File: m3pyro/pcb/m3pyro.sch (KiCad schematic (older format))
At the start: 54 parts, among them IC1 STM32F405RxTx, IC2 MCP2562, J10 WEST BOT, J11 EAST TOP, J12 EAST BOT, J9 WEST TOP, Q1 2FET2, Q2 2FET2, Q3 2FET2, Q4 2FET2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

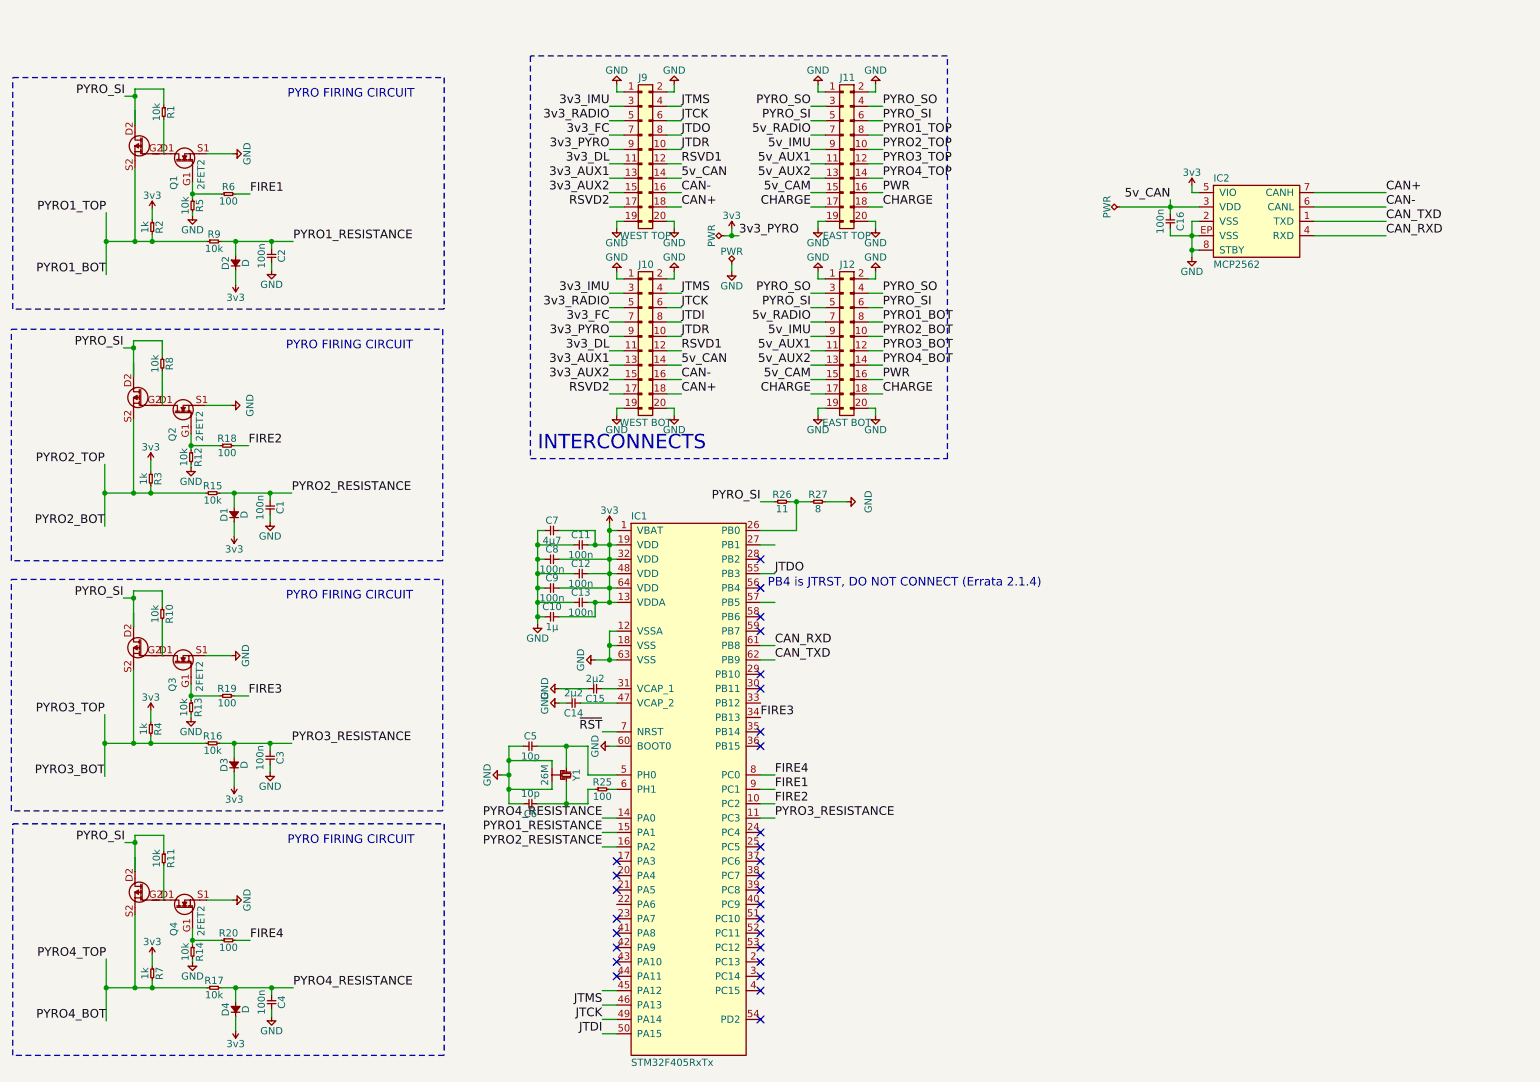
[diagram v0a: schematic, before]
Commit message: schematic in line?
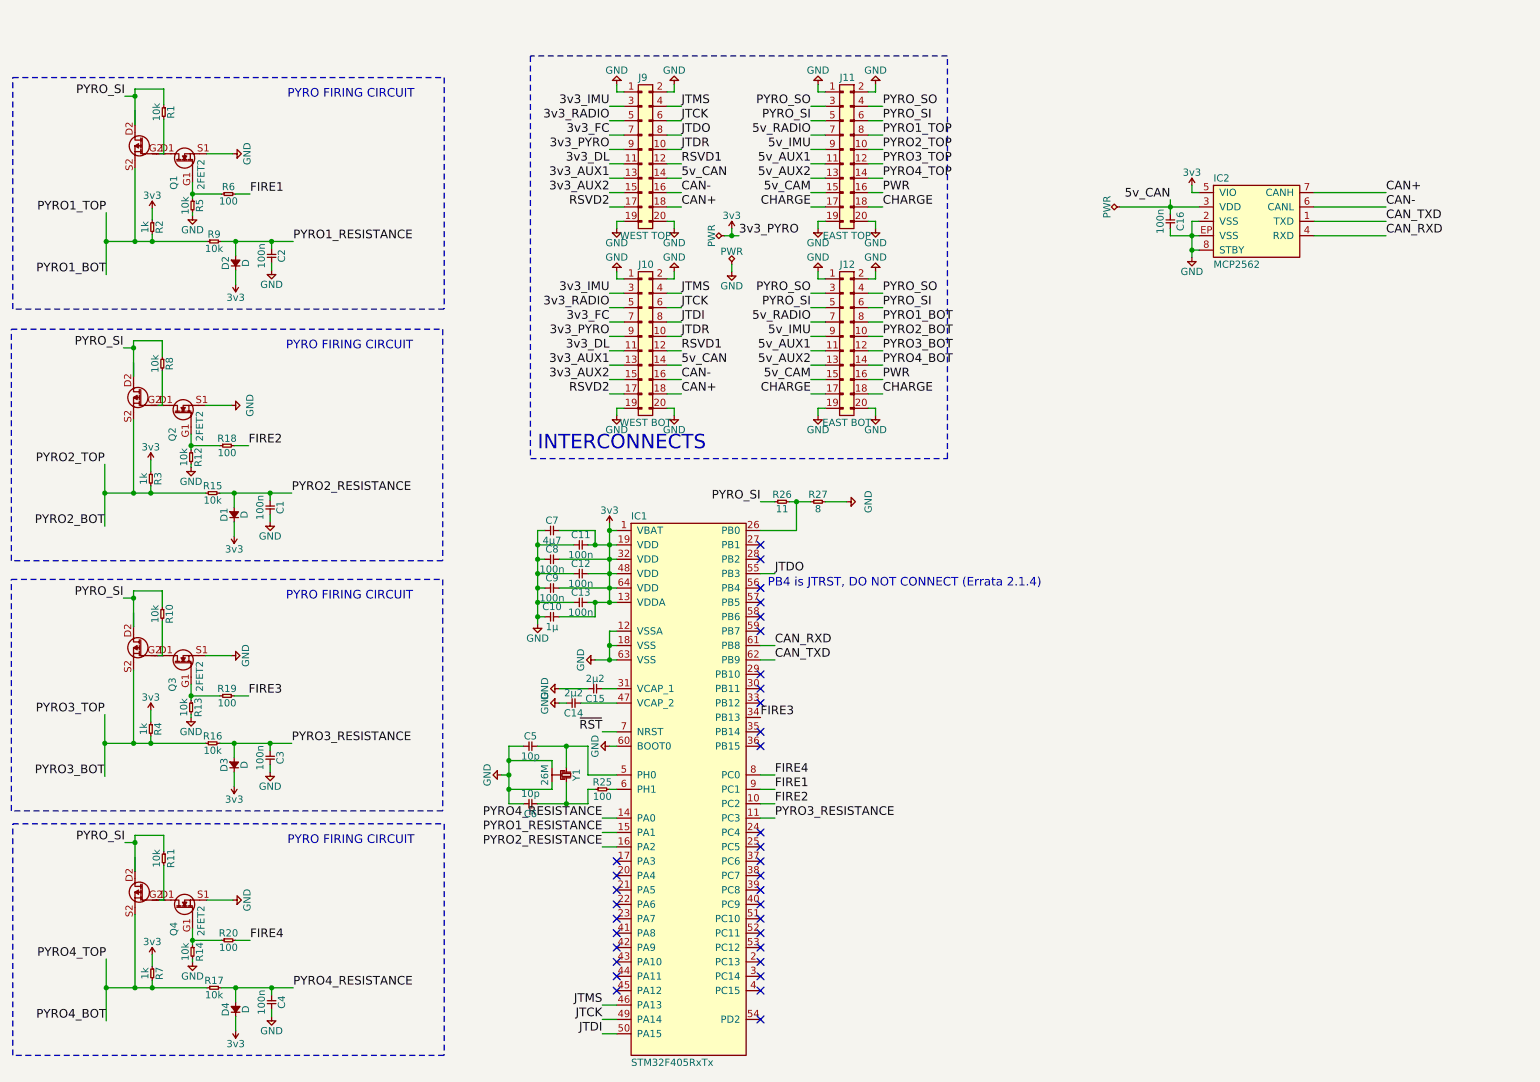
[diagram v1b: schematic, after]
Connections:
- net at Q1.D1, R1.2: now also Q1.G2
- net at Q2.D1, R8.2: now also Q2.G2
- net at Q3.D1, R10.2: now also Q3.G2
- net at Q4.D1, R11.2: now also Q4.G2
- no-connect marks 29 -> 34
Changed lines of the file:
@@
 	4750 7250 4650 7250
-Wire Wire Line
-	5750 4050 5850 4050
-Wire Wire Line
-	4650 5150 4750 5150
 Wire Wire Line
 	4700 5250 4750 5250
@@
 	5750 4550 5850 4550
 Wire Wire Line
-	4650 6950 4750 6950
-Wire Wire Line
 	4650 5850 4750 5850
 Wire Wire Line
@@
 Wire Wire Line
 	9600 1700 10100 1700
-Wire Wire Line
-	5750 3850 5850 3850
-Wire Wire Line
-	5750 4250 5850 4250
 Wire Wire Line
 	2350 1740 2350 1790
@@
 Wire Wire Line
 	1400 680  1400 930
+Wire Wire Line
+	1390 2430 1390 2680
+Wire Wire Line
+	1320 2480 1390 2480
+Connection ~ 1390 2480
+$Comp
+L 2FET2 Q3
+U 1 1 5782F422
+P 1490 4220
+F 0 "Q3" H 840 4050 50  0000 L CNN
+F 1 "2FET2" H 840 3860 50  0000 L CNN
+F 2 "m3pyro:PowerPAK-SC-70-6-DUAL" H 1090 4020 50  0001 C CNN
+F 3 "" H 1090 4020 50  0001 C CNN
+	1    1490 4220
+	0    -1   -1   0
+$EndComp
+$Comp
+L 2FET2 Q4
+U 1 1 5782F916
+P 1500 5920
+F 0 "Q4" H 850 5750 50  0000 L CNN
+F 1 "2FET2" H 850 5560 50  0000 L CNN
+F 2 "m3pyro:PowerPAK-SC-70-6-DUAL" H 1100 5720 50  0001 C CNN
+F 3 "" H 1100 5720 50  0001 C CNN
+	1    1500 5920
+	0    -1   -1   0
+$EndComp
+Wire Wire Line
+	1570 1130 1600 1130
+Wire Wire Line
+	1560 2880 1590 2880
+Wire Wire Line
+	1560 4620 1590 4620
+Wire Wire Line
+	1570 6320 1600 6320
 $Comp
 L 2FET2 Q2
@@
 	0    -1   -1   0
 $EndComp
-Wire Wire Line
-	1390 2430 1390 2680
-Wire Wire Line
-	1320 2480 1390 2480
-Connection ~ 1390 2480
-$Comp
-L 2FET2 Q3
-U 1 1 5782F422
-P 1490 4220
-F 0 "Q3" H 840 4050 50  0000 L CNN
-F 1 "2FET2" H 840 3860 50  0000 L CNN
-F 2 "m3pyro:PowerPAK-SC-70-6-DUAL" H 1090 4020 50  0001 C CNN
-F 3 "" H 1090 4020 50  0001 C CNN
-	1    1490 4220
-	0    -1   -1   0
-$EndComp
-$Comp
-L 2FET2 Q4
-U 1 1 5782F916
-P 1500 5920
-F 0 "Q4" H 850 5750 50  0000 L CNN
-F 1 "2FET2" H 850 5560 50  0000 L CNN
-F 2 "m3pyro:PowerPAK-SC-70-6-DUAL" H 1100 5720 50  0001 C CNN
-F 3 "" H 1100 5720 50  0001 C CNN
-	1    1500 5920
-	0    -1   -1   0
-$EndComp
+NoConn ~ 4750 6350
+NoConn ~ 4750 6950
+NoConn ~ 5750 4950
+Wire Wire Line
+	5750 4050 5850 4050
+NoConn ~ 5750 3850
+NoConn ~ 5750 4250
+Wire Wire Line
+	4750 5150 4650 5150
 $EndSCHEMATC

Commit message: further updates
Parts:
- removed Q1, Q2, Q3, Q4: 2FET2, m3pyro:PowerPAK-SC-70-6-DUAL, symbol 2FET2
- added C17: 100n, agg:0402, symbol C
- added D5: D, agg:0402, symbol D
- added Q1, Q2, Q3, Q4, Q5: 2FET3, m3pyro:PowerPAK-SC-70-6-DUAL, symbol 2FET3
- added R21: 1k, agg:0402, symbol R
- added R22, R23, R24: 10k, agg:0402, symbol R
- added R28: 100, agg:0402, symbol R
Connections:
- net labels added: FIRE5, PYRO5, PYRO5_RESISTANCE
- wire segments 260 -> 280
- no-connect marks 34 -> 33

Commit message: final schematic
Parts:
- removed C17: 100n, agg:0402, symbol C
- removed D5: D, agg:0402, symbol D
- removed Q5: 2FET3, m3pyro:PowerPAK-SC-70-6-DUAL, symbol 2FET3
- removed R21: 1k, agg:0402, symbol R
- removed R22, R23, R24: 10k, agg:0402, symbol R
- removed R28: 100, agg:0402, symbol R
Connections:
- net labels removed: FIRE5, PYRO5, PYRO5_RESISTANCE
- wire segments 280 -> 259
- no-connect marks 33 -> 35
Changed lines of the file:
@@
 LIBS:m3pyro-rescue
 LIBS:agg-kicad
+LIBS:extended pyro library
 LIBS:m3pyro-cache
 EELAYER 25 0
@@
 PYRO2_BOT
 Text Label 6600 2300 0    60   ~ 0
-PYRO5
+PYRO1_BOT
 Text Notes 4200 3200 0    100  ~ 0
 INTERCONNECTS
@@
 	0    -1   -1   0
 $EndComp
-$Comp
-L R R21
-U 1 1 57881E0A
-P 8970 5730
-F 0 "R21" H 9020 5780 50  0000 C CNN
-F 1 "1k" H 9020 5680 50  0000 C CNN
-F 2 "agg:0402" H 8970 5730 50  0001 C CNN
-F 3 "" H 8970 5730 50  0001 C CNN
-	1    8970 5730
-	0    1    1    0
-$EndComp
-$Comp
-L 3v3 #PWR052
-U 1 1 57881E10
-P 8970 5650
-F 0 "#PWR052" H 8970 5760 50  0001 L CNN
-F 1 "3v3" H 8970 5740 50  0000 C CNN
-F 2 "" H 8970 5650 60  0000 C CNN
-F 3 "" H 8970 5650 60  0000 C CNN
-	1    8970 5650
-	1    0    0    -1
-$EndComp
-$Comp
-L D D5
-U 1 1 57881E16
-P 9550 6080
-F 0 "D5" H 9600 6150 50  0000 C CNN
-F 1 "D" H 9600 6010 50  0000 C CNN
-F 2 "agg:0402" H 9550 6080 50  0001 C CNN
-F 3 "" H 9550 6080 50  0001 C CNN
-	1    9550 6080
-	0    -1   -1   0
-$EndComp
-$Comp
-L 3v3 #PWR053
-U 1 1 57881E1C
-P 9550 6180
-F 0 "#PWR053" H 9550 6290 50  0001 L CNN
-F 1 "3v3" H 9550 6270 50  0000 C CNN
-F 2 "" H 9550 6180 60  0000 C CNN
-F 3 "" H 9550 6180 60  0000 C CNN
-	1    9550 6180
-	-1   0    0    1
-$EndComp
-$Comp
-L R R22
-U 1 1 57881E22
-P 9050 4930
-F 0 "R22" H 9100 4980 50  0000 C CNN
-F 1 "10k" H 9100 4880 50  0000 C CNN
-F 2 "agg:0402" H 9050 4930 50  0001 C CNN
-F 3 "" H 9050 4930 50  0001 C CNN
-	1    9050 4930
-	0    1    1    0
-$EndComp
-$Comp
-L R R23
-U 1 1 57881E28
-P 9250 5580
-F 0 "R23" H 9300 5630 50  0000 C CNN
-F 1 "10k" H 9300 5530 50  0000 C CNN
-F 2 "agg:0402" H 9250 5580 50  0001 C CNN
-F 3 "" H 9250 5580 50  0001 C CNN
-	1    9250 5580
-	0    1    1    0
-$EndComp
-$Comp
-L R R28
-U 1 1 57881E2E
-P 9450 5550
-F 0 "R28" H 9500 5600 50  0000 C CNN
-F 1 "100" H 9500 5500 50  0000 C CNN
-F 2 "agg:0402" H 9450 5550 50  0001 C CNN
-F 3 "" H 9450 5550 50  0001 C CNN
-	1    9450 5550
-	1    0    0    -1
-$EndComp
-$Comp
-L GND #PWR054
-U 1 1 57881E34
-P 9250 5700
-F 0 "#PWR054" H 9120 5740 50  0001 L CNN
-F 1 "GND" H 9250 5600 50  0000 C CNN
-F 2 "" H 9250 5700 60  0000 C CNN
-F 3 "" H 9250 5700 60  0000 C CNN
-	1    9250 5700
-	1    0    0    -1
-$EndComp
-Text Label 9650 5550 0    60   ~ 0
-FIRE5
-Text Notes 9910 4890 0    60   ~ 0
-PYRO FIRING CIRCUIT
-Text Label 8650 5680 2    60   ~ 0
-PYRO5
-Text Label 8780 4870 2    60   ~ 0
-PYRO_SI
-Text Label 5750 5450 0    60   ~ 0
-PYRO5_RESISTANCE
-$Comp
-L GND #PWR055
-U 1 1 57881E3F
-P 9800 6080
-F 0 "#PWR055" H 9670 6120 50  0001 L CNN
-F 1 "GND" H 9800 5980 50  0000 C CNN
-F 2 "" H 9800 6080 60  0000 C CNN
-F 3 "" H 9800 6080 60  0000 C CNN
-	1    9800 6080
-	1    0    0    -1
-$EndComp
-$Comp
-L R R24
-U 1 1 57881E45
-P 9350 5880
-F 0 "R24" H 9400 5930 50  0000 C CNN
-F 1 "10k" H 9400 5830 50  0000 C CNN
-F 2 "agg:0402" H 9350 5880 50  0001 C CNN
-F 3 "" H 9350 5880 50  0001 C CNN
-	1    9350 5880
-	1    0    0    -1
-$EndComp
-$Comp
-L C C17
-U 1 1 57881E4B
-P 9800 5930
-F 0 "C17" H 9850 6000 50  0000 C CNN
-F 1 "100n" H 9850 5860 50  0000 C CNN
-F 2 "agg:0402" H 9800 5930 50  0001 C CNN
-F 3 "" H 9800 5930 50  0001 C CNN
-	1    9800 5930
-	0    1    1    0
-$EndComp
-Text Label 8650 6110 2    60   ~ 0
-PYRO5
-Connection ~ 8970 5880
-Wire Wire Line
-	9550 5550 9650 5550
-Wire Wire Line
-	9250 5550 9450 5550
-Wire Wire Line
-	8970 5650 8970 5730
-Connection ~ 8850 5880
-Wire Wire Line
-	9800 5880 9800 5930
-Connection ~ 9800 5880
-Wire Wire Line
-	9800 6030 9800 6080
-Wire Wire Line
-	8650 5880 9350 5880
-Wire Notes Line
-	11000 4740 11000 6350
-Wire Notes Line
-	11000 6350 8000 6350
-Wire Wire Line
-	9550 5880 9550 5980
-Connection ~ 9550 5880
-Wire Wire Line
-	9550 6080 9550 6180
-Wire Notes Line
-	8000 6350 8000 4740
-Wire Wire Line
-	9450 5880 9950 5880
-Connection ~ 8650 5880
-Wire Wire Line
-	8970 5880 8970 5830
-Connection ~ 8850 4870
-Connection ~ 9250 5550
-Wire Wire Line
-	9250 5470 9250 5580
-Wire Wire Line
-	9050 5270 9050 5030
-Wire Wire Line
-	9350 5270 9530 5270
-$Comp
-L GND #PWR056
-U 1 1 57881E69
-P 9530 5270
-F 0 "#PWR056" H 9400 5310 50  0001 L CNN
-F 1 "GND" H 9530 5170 50  0000 C CNN
-F 2 "" H 9530 5270 60  0000 C CNN
-F 3 "" H 9530 5270 60  0000 C CNN
-	1    9530 5270
-	0    -1   -1   0
-$EndComp
-Wire Wire Line
-	8850 4820 8850 5070
-Wire Wire Line
-	8850 4820 9050 4820
-Wire Wire Line
-	9050 4820 9050 4930
-Wire Wire Line
-	8780 4870 8850 4870
-Wire Wire Line
-	9250 5680 9250 5700
-Wire Wire Line
-	8850 5370 8850 5880
-Wire Notes Line
-	8000 4740 11000 4740
-Wire Wire Line
-	8650 5680 8650 6110
-Wire Wire Line
-	9020 5270 9050 5270
-$Comp
-L 2FET3 Q5
-U 1 1 57881E78
-P 8950 4870
-F 0 "Q5" H 8300 4700 50  0000 L CNN
-F 1 "2FET3" H 8300 4510 50  0000 L CNN
-F 2 "m3pyro:PowerPAK-SC-70-6-DUAL" H 8550 4670 50  0001 C CNN
-F 3 "" H 8550 4670 50  0001 C CNN
-	1    8950 4870
-	0    -1   -1   0
-$EndComp
-Text Label 4750 6050 2    60   ~ 0
-FIRE5
-Text Label 9950 5880 0    60   ~ 0
-PYRO5_RESISTANCE
+NoConn ~ 5750 5450
+NoConn ~ 4750 6050
 $EndSCHEMATC
